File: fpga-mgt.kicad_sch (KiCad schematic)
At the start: 11 parts, among them U4 XC7K160T-FFG676

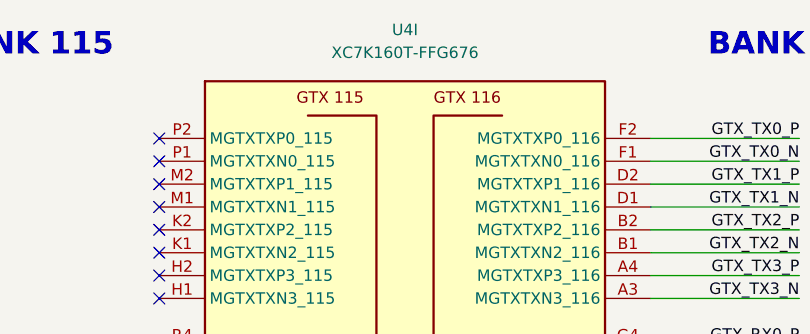
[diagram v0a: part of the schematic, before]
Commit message: Fix FPGA properties from the standardized library, update SO-DIMM symbol
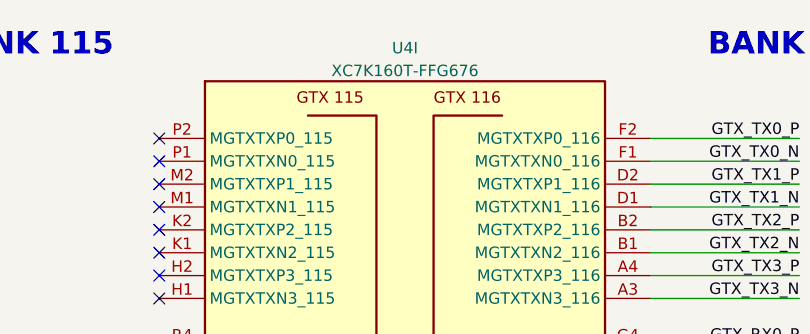
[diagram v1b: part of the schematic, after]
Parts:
- U4: footprint sodimm-ddr5-tester-footprints:BGA-676_27x27mm_Layout26x26_P1X1mm -> antmicro-footprints:BGA-676_27x27mm_Layout26x26_P1X1mm; symbol sodimm-ddr5-tester:XC7K160T-FFG676 -> antmicroMicrocontrollers:XC7K160T-FFG676; Manufacturer Xilinx -> AMD-Xilinx
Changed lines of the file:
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@@
     (pin "2")
   )
-  (symbol (lib_id "sodimm-ddr5-tester:XC7K160T-FFG676") (at 172.085 53.34 0) (unit 9)
+  (symbol (lib_id "antmicroMicrocontrollers:XC7K160T-FFG676") (at 172.085 53.34 0) (unit 9)
     (in_bom yes) (on_board yes) (fields_autoplaced)
-    (property "Reference" "U4" (id 0) (at 199.39 41.275 0))
-    (property "Value" "XC7K160T-FFG676" (id 1) (at 199.39 43.815 0)
+    (property "Reference" "U4" (id 0) (at 199.39 43.2984 0))
+    (property "Value" "XC7K160T-FFG676" (id 1) (at 199.39 45.8287 0)
       (effects (font (size 1.27 1.27) (thickness 0.15)))
     )
-    (property "Footprint" "sodimm-ddr5-tester-footprints:BGA-676_27x27mm_Layout26x26_P1X1mm" (id 2) (at 240.665 55.88 0)
+    (property "Footprint" "antmicro-footprints:BGA-676_27x27mm_Layout26x26_P1X1mm" (id 2) (at 240.665 55.88 0)
       (effects (font (size 1.27 1.27) (thickness 0.15)) (justify left bottom) hide)
     )
@@
       (effects (font (size 1.27 1.27) (thickness 0.15)) (justify left bottom) hide)
     )
-    (property "Manufacturer" "Xilinx" (id 7) (at 172.085 53.34 0)
+    (property "Manufacturer" "AMD-Xilinx" (id 7) (at 172.085 53.34 0)
       (effects (font (size 1.27 1.27)) hide)
     )

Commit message: Loclib of the project
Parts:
- U4: footprint antmicro-footprints:BGA-676_27x27mm_Layout26x26_P1X1mm -> sodimm-ddr5-tester-footprints:BGA-676_27x27mm_Layout26x26_P1X1mm; symbol antmicroMicrocontrollers:XC7K160T-FFG676 -> sodimm-ddr5-tester:XC7K160T-FFG676

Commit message: Finish schematic cleanup
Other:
- note added: "MGT Interface"
- moved on the sheet: C222, C223, C226, C227, C228, C229, C230, C231, C232, C233, U4I

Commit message: [#57478] ohp release
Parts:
- C222, C223, C226, C227, C228, C229, C230, C231, C232, C233: footprint sodimm-ddr5-tester-footprints:C_0402_1005Metric -> antmicro-footprints:C_0402_1005Metric; symbol sodimm-ddr5-tester:C_100n_0402 -> antmicroCapacitors0402:C_100n_0402
- U4: footprint sodimm-ddr5-tester-footprints:BGA-676_27x27mm_Layout26x26_P1X1mm -> antmicro-footprints:BGA-676_27x27mm_Layout26x26_P1x1mm_FFG676; symbol sodimm-ddr5-tester:XC7K160T-FFG676 -> antmicroFPGAChips:XC7K160T-FFG676
